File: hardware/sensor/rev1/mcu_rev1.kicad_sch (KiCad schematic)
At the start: 27 parts, among them IC1 STM8L051F3P6, J1 22-28-4044, J2 M20-9770342

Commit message: EG-49 ERC with no errors.
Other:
- moved on the sheet: TP12, TP13
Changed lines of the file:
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@@
 	)
 	(junction
+		(at 78.74 115.57)
+		(diameter 0)
+		(color 0 0 0 0)
+	)
+	(junction
 		(at 58.42 24.13)
 		(diameter 0)
@@
 	)
 	(junction
+		(at 193.04 71.12)
+		(diameter 0)
+		(color 0 0 0 0)
+	)
+	(junction
 		(at 133.35 168.91)
 		(diameter 0)
@@
 	)
 	(junction
+		(at 170.18 71.12)
+		(diameter 0)
+		(color 0 0 0 0)
+	)
+	(junction
 		(at 36.83 24.13)
 		(diameter 0)
@@
 	)
 	(junction
-		(at 102.87 26.67)
-		(diameter 0)
-		(color 0 0 0 0)
-	)
-	(junction
 		(at 146.05 158.75)
 		(diameter 0)
@@
 	(wire
 		(pts
-			(xy 172.72 87.63) (xy 172.72 96.52)
+			(xy 170.18 87.63) (xy 170.18 96.52)
 		)
 		(stroke
@@
 	(wire
 		(pts
-			(xy 93.98 26.67) (xy 102.87 26.67)
+			(xy 78.74 115.57) (xy 78.74 119.38)
 		)
 		(stroke
@@
 	(wire
 		(pts
-			(xy 166.37 71.12) (xy 172.72 71.12)
+			(xy 166.37 71.12) (xy 170.18 71.12)
 		)
 		(stroke
@@
 	(wire
 		(pts
-			(xy 78.74 119.38) (xy 90.17 119.38)
-		)
-		(stroke
-			(width 0)
-			(type default)
-		)
-	)
-	(wire
-		(pts
 			(xy 62.23 119.38) (xy 62.23 123.19)
 		)
@@
 	(wire
 		(pts
-			(xy 93.98 22.86) (xy 93.98 26.67)
+			(xy 170.18 71.12) (xy 172.72 71.12)
 		)
 		(stroke
@@
 	(wire
 		(pts
-			(xy 187.96 64.77) (xy 187.96 71.12)
+			(xy 100.33 91.44) (xy 100.33 96.52)
 		)
 		(stroke
@@
 	(wire
 		(pts
-			(xy 100.33 91.44) (xy 100.33 96.52)
+			(xy 60.96 148.59) (xy 83.82 148.59)
 		)
 		(stroke
@@
 	(wire
 		(pts
-			(xy 60.96 148.59) (xy 83.82 148.59)
+			(xy 36.83 36.83) (xy 39.37 36.83)
 		)
 		(stroke
@@
 	(wire
 		(pts
-			(xy 36.83 36.83) (xy 39.37 36.83)
+			(xy 83.82 166.37) (xy 78.74 166.37)
 		)
 		(stroke
@@
 	(wire
 		(pts
-			(xy 166.37 85.09) (xy 172.72 85.09)
+			(xy 187.96 82.55) (xy 187.96 85.09)
 		)
 		(stroke
@@
 	(wire
 		(pts
-			(xy 83.82 166.37) (xy 78.74 166.37)
+			(xy 62.23 119.38) (xy 78.74 119.38)
 		)
 		(stroke
@@
 	(wire
 		(pts
-			(xy 187.96 82.55) (xy 187.96 85.09)
+			(xy 187.96 71.12) (xy 187.96 74.93)
 		)
 		(stroke
@@
 	(wire
 		(pts
-			(xy 62.23 119.38) (xy 78.74 119.38)
+			(xy 67.31 78.74) (xy 67.31 87.63)
 		)
 		(stroke
@@
 	(wire
 		(pts
-			(xy 187.96 71.12) (xy 187.96 74.93)
+			(xy 100.33 29.21) (xy 106.68 29.21)
 		)
 		(stroke
@@
 	(wire
 		(pts
-			(xy 67.31 78.74) (xy 67.31 87.63)
+			(xy 39.37 24.13) (xy 39.37 25.4)
 		)
 		(stroke
@@
 	(wire
 		(pts
-			(xy 100.33 29.21) (xy 106.68 29.21)
+			(xy 29.21 78.74) (xy 29.21 86.36)
 		)
 		(stroke
@@
 	(wire
 		(pts
-			(xy 39.37 24.13) (xy 39.37 25.4)
+			(xy 193.04 71.12) (xy 199.39 71.12)
 		)
 		(stroke
@@
 	(wire
 		(pts
-			(xy 29.21 78.74) (xy 29.21 86.36)
+			(xy 166.37 87.63) (xy 170.18 87.63)
 		)
 		(stroke
@@
 	(wire
 		(pts
-			(xy 166.37 87.63) (xy 172.72 87.63)
+			(xy 193.04 64.77) (xy 193.04 71.12)
 		)
 		(stroke
@@
 	(wire
 		(pts
-			(xy 78.74 111.76) (xy 78.74 119.38)
+			(xy 78.74 111.76) (xy 78.74 115.57)
 		)
 		(stroke
@@
 	(wire
 		(pts
+			(xy 66.04 115.57) (xy 78.74 115.57)
+		)
+		(stroke
+			(width 0)
+			(type default)
+		)
+	)
+	(wire
+		(pts
 			(xy 102.87 26.67) (xy 102.87 22.86)
 		)
@@
 	(wire
 		(pts
+			(xy 170.18 85.09) (xy 170.18 71.12)
+		)
+		(stroke
+			(width 0)
+			(type default)
+		)
+	)
+	(wire
+		(pts
 			(xy 17.78 24.13) (xy 26.67 24.13)
 		)
@@
 	(wire
 		(pts
-			(xy 172.72 85.09) (xy 172.72 71.12)
+			(xy 60.96 151.13) (xy 83.82 151.13)
 		)
 		(stroke
@@
 	(wire
 		(pts
-			(xy 60.96 151.13) (xy 83.82 151.13)
+			(xy 146.05 158.75) (xy 160.02 158.75)
 		)
 		(stroke
@@
 	(wire
 		(pts
-			(xy 146.05 158.75) (xy 160.02 158.75)
+			(xy 74.93 177.8) (xy 74.93 168.91)
 		)
 		(stroke
@@
 	(wire
 		(pts
-			(xy 74.93 177.8) (xy 74.93 168.91)
+			(xy 78.74 119.38) (xy 78.74 166.37)
 		)
 		(stroke
@@
 	(wire
 		(pts
-			(xy 78.74 119.38) (xy 78.74 166.37)
+			(xy 187.96 71.12) (xy 193.04 71.12)
 		)
 		(stroke
@@
 	(wire
 		(pts
-			(xy 187.96 71.12) (xy 199.39 71.12)
+			(xy 166.37 85.09) (xy 170.18 85.09)
 		)
 		(stroke
@@
 	)
 	(symbol
-		(lib_id "power:PWR_FLAG")
-		(at 93.98 22.86 0)
-		(unit 1)
-		(exclude_from_sim no)
-		(in_bom yes)
-		(on_board yes)
-		(dnp no)
-		(fields_autoplaced yes)
-		(property "Reference" "#FLG03"
-			(at 93.98 20.955 0)
-			(effects
-				(font
-					(size 1.27 1.27)
-				)
-				(hide yes)
-			)
-		)
-		(property "Value" "PWR_FLAG"
-			(at 93.98 17.78 0)
-			(effects
-				(font
-					(size 1.27 1.27)
-				)
-			)
-		)
-		(property "Footprint" ""
-			(at 93.98 22.86 0)
-			(effects
-				(font
-					(size 1.27 1.27)
-				)
-				(hide yes)
-			)
-		)
-		(property "Datasheet" "~"
-			(at 93.98 22.86 0)
-			(effects
-				(font
-					(size 1.27 1.27)
-				)
-				(hide yes)
-			)
-		)
-		(property "Description" "Special symbol for telling ERC where power comes from"
-			(at 93.98 22.86 0)
-			(effects
-				(font
-					(size 1.27 1.27)
-				)
-				(hide yes)
-			)
-		)
-		(pin "1"
-		)
-		(instances
-			(project "mcu_rev1"
-				(path "/c9ab58dc-163d-4c4e-8d12-3a07665777cf"
-					(reference "#FLG?")
-					(unit 1)
-				)
-			)
-			(project "sensor_rev1"
-				(path "/d3cb7130-decc-418b-958e-e5d84a8d867f/ec220677-d66d-4ee1-961f-1c93fb46783a"
-					(reference "#FLG03")
-					(unit 1)
-				)
-			)
-		)
-	)
-	(symbol
 		(lib_id "power:GND")
 		(at 171.45 34.29 0)
@@
 	(symbol
 		(lib_id "Connector:TestPoint")
-		(at 187.96 64.77 0)
+		(at 193.04 64.77 0)
 		(unit 1)
 		(exclude_from_sim no)
@@
 		(fields_autoplaced yes)
 		(property "Reference" "TP12"
-			(at 190.5 60.1979 0)
+			(at 195.58 60.1979 0)
 			(effects
 				(font
@@
 		)
 		(property "Value" "REED"
-			(at 190.5 62.7379 0)
+			(at 195.58 62.7379 0)
 			(effects
 				(font
@@
 		)
 		(property "Footprint" "TestPoint:TestPoint_Pad_D1.0mm"
-			(at 193.04 64.77 0)
+			(at 198.12 64.77 0)
 			(effects
 				(font
@@
 		)
 		(property "Datasheet" "~"
-			(at 193.04 64.77 0)
+			(at 198.12 64.77 0)
 			(effects
 				(font
@@
 		)
 		(property "Description" "test point"
-			(at 187.96 64.77 0)
+			(at 193.04 64.77 0)
 			(effects
 				(font
@@
 	(symbol
 		(lib_id "power:GND")
-		(at 172.72 96.52 0)
+		(at 170.18 96.52 0)
 		(unit 1)
 		(exclude_from_sim no)
@@
 		(fields_autoplaced yes)
 		(property "Reference" "#PWR013"
-			(at 172.72 102.87 0)
+			(at 170.18 102.87 0)
 			(effects
 				(font
@@
 		)
 		(property "Value" "GND"
-			(at 172.72 101.6 0)
+			(at 170.18 101.6 0)
 			(effects
 				(font
@@
 		)
 		(property "Footprint" ""
-			(at 172.72 96.52 0)
+			(at 170.18 96.52 0)
 			(effects
 				(font
@@
 		)
 		(property "Datasheet" ""
-			(at 172.72 96.52 0)
+			(at 170.18 96.52 0)
 			(effects
 				(font
@@
 		)
 		(property "Description" "Power symbol creates a global label with name \"GND\" , ground"
-			(at 172.72 96.52 0)
+			(at 170.18 96.52 0)
 			(effects
 				(font
@@
 	(symbol
 		(lib_id "Connector:TestPoint")
-		(at 90.17 119.38 270)
+		(at 66.04 115.57 90)
 		(unit 1)
 		(exclude_from_sim no)
@@
 		(fields_autoplaced yes)
 		(property "Reference" "TP13"
-			(at 95.25 118.1099 90)
+			(at 62.738 110.49 90)
 			(effects
 				(font
 					(size 1.27 1.27)
 				)
-				(justify left)
 			)
 		)
 		(property "Value" "MCU_VDD"
-			(at 95.25 120.6499 90)
+			(at 62.738 113.03 90)
 			(effects
 				(font
 					(size 1.27 1.27)
 				)
-				(justify left)
 			)
 		)
 		(property "Footprint" "TestPoint:TestPoint_Pad_D1.0mm"
-			(at 90.17 124.46 0)
+			(at 66.04 110.49 0)
 			(effects
 				(font
@@
 		)
 		(property "Datasheet" "~"
-			(at 90.17 124.46 0)
+			(at 66.04 110.49 0)
 			(effects
 				(font
@@
 		)
 		(property "Description" "test point"
-			(at 90.17 119.38 0)
+			(at 66.04 115.57 0)
 			(effects
 				(font

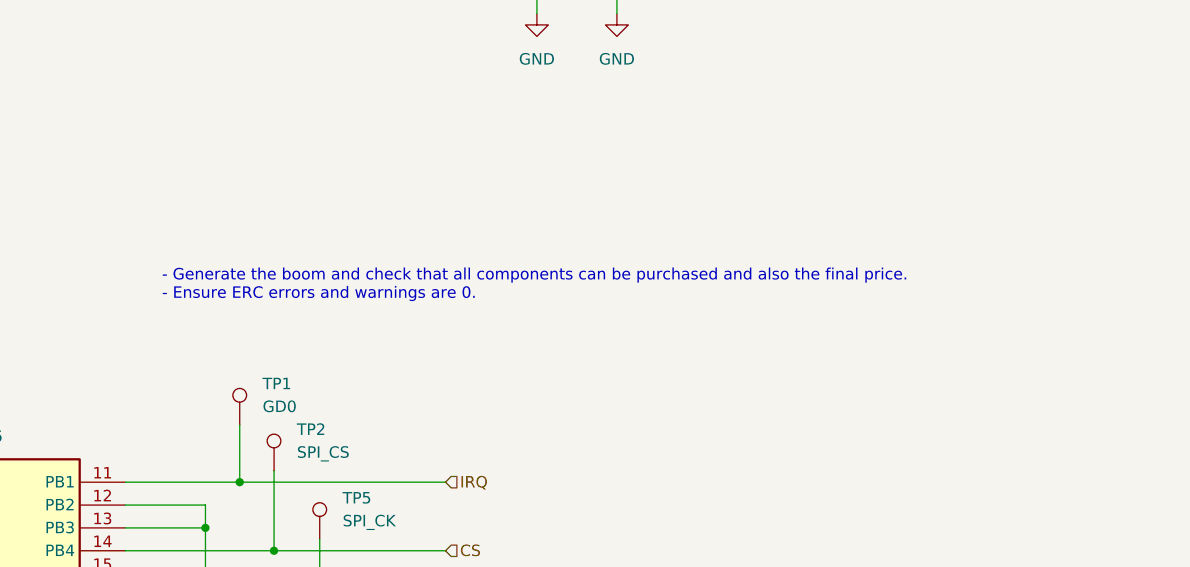
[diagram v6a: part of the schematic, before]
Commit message: EG-49 No ERC warnings.
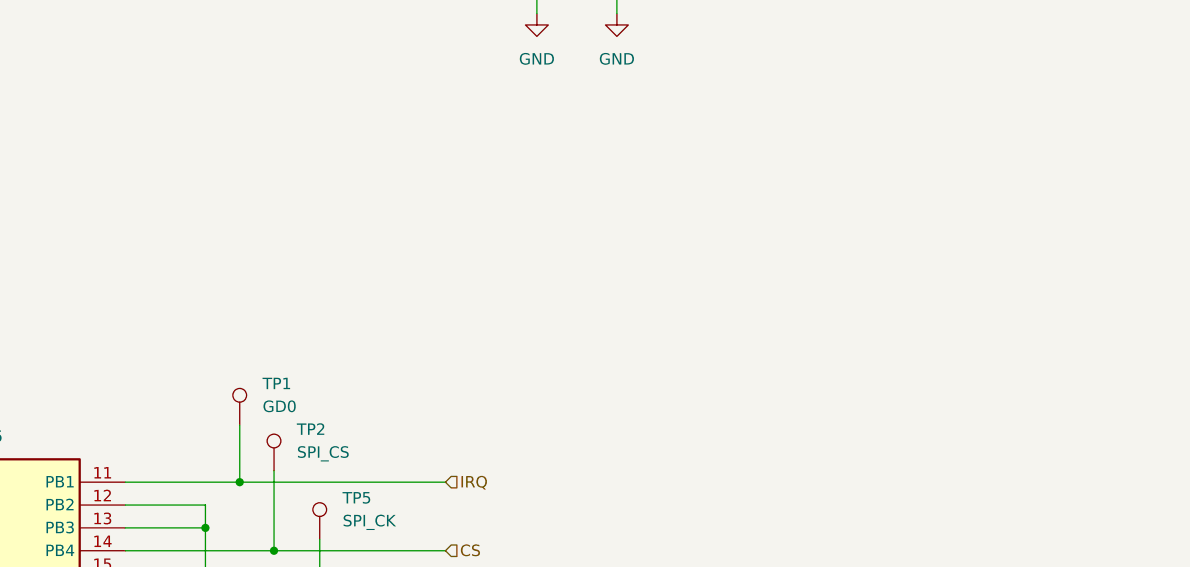
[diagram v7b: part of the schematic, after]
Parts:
- J2: Manufacturer (none) -> Harwin; Manufacturer Part Number (none) -> M20-9770342; Supplier Link (none) -> https://www.mouser.co.uk/ProductDetail/Harwin/M20-9770342?q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
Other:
- note removed: "- Generate the boom and check that all components can be purchased and also the final price. - Ensure ERC errors and warnings are 0."
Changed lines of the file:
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@@
-		)
-	)
-	(text "- Generate the boom and check that all components can be purchased and also the final price.\n- Ensure ERC errors and warnings are 0."
-		(exclude_from_sim no)
-		(at 128.524 126.746 0)
-		(effects
-			(font
-				(size 1.27 1.27)
-			)
-			(justify left)
 		)
 	)
@@
 			(at 190.5 820.32 0)
 			(effects
+				(font
+					(size 1.27 1.27)
+				)
+				(justify left top)
+				(hide yes)
+			)
+		)
+		(property "Supplier Link" "https://www.mouser.co.uk/ProductDetail/Harwin/M20-9770342?qs=Jph8NoUxIfVskiTzAX%252BIFA%3D%3D"
+			(at 190.5 620.32 0)
+			(effects
+				(font
+					(size 1.27 1.27)
+				)
+				(justify left top)
+				(hide yes)
+			)
+		)
+		(property "Manufacturer" "Harwin"
+			(at 190.5 720.32 0)
+			(effects
+				(font
+					(size 1.27 1.27)
+				)
+				(justify left top)
+				(hide yes)
+			)
+		)
+		(property "Manufacturer Part Number" "M20-9770342"
+			(at 190.5 820.32 0)
+			(effects

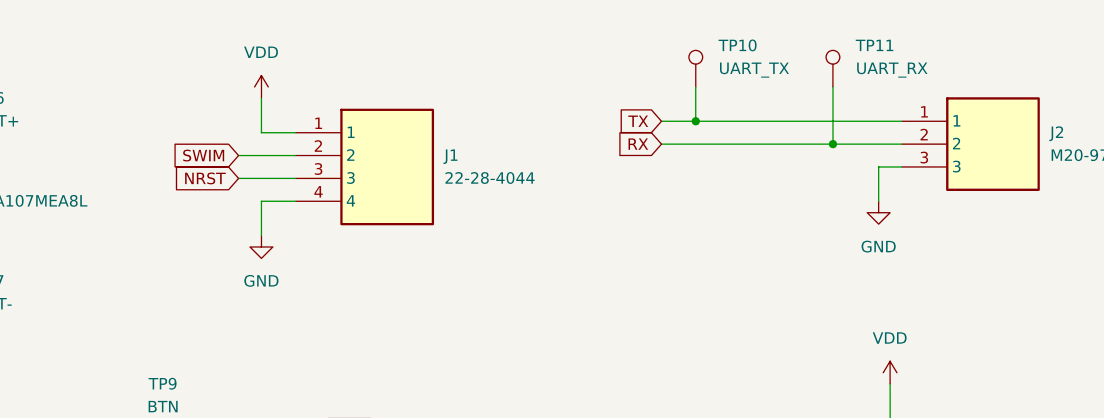
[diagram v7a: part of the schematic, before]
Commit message: EG-50 Components ready to be connected.
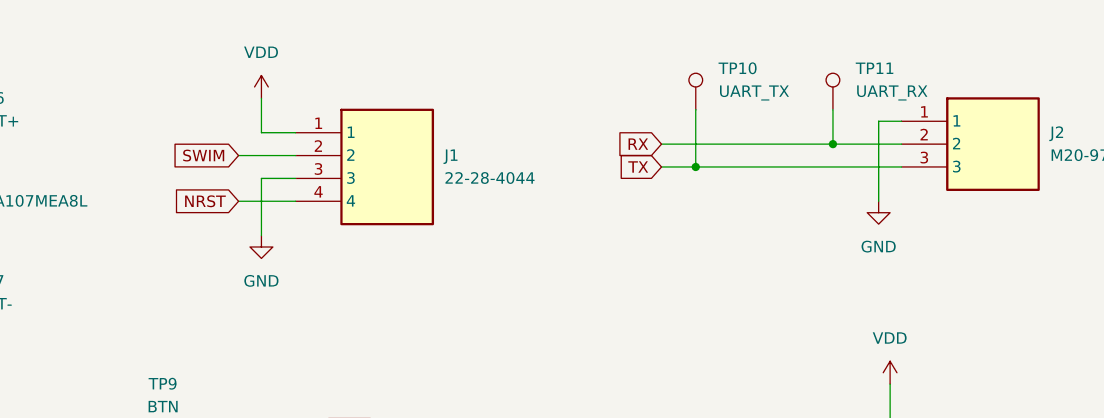
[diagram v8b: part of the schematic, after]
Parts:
- S1, S3: Mouser Part Number (none) -> 876-GP560/20-25; Mouser Price/Stock (none) -> https://pt.mouser.com/en/ProductDetail/MEDER-electronic/GP5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
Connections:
- net GND: now also J1.3, J2.1; no longer J1.4, J2.3
- net NRST: now also J1.4; no longer J1.3
- net TX: now also J2.3; no longer J2.1
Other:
- moved on the sheet: TP10, TP11
